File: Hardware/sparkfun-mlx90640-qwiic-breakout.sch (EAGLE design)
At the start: 23 parts, among them J2 SMD, J3 PTH, J4 SMD, U1 MLX90640

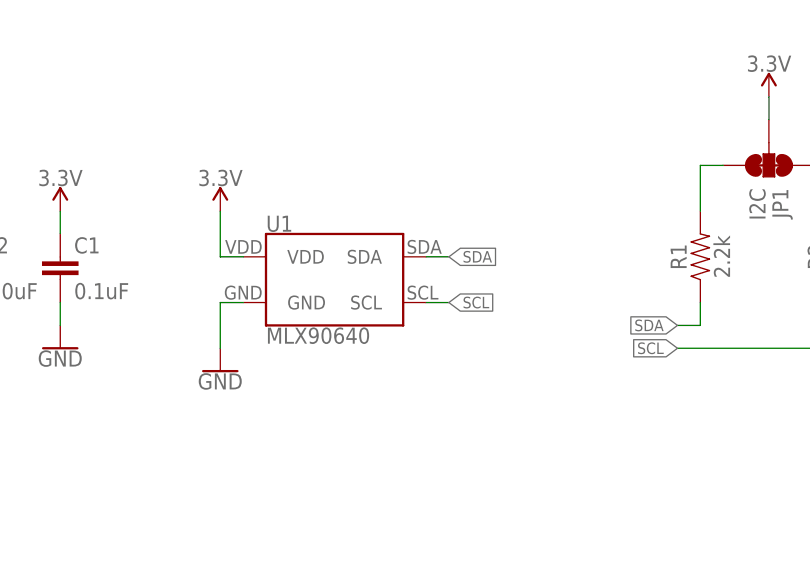
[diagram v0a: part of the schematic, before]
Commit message: Adding I2C address to schematic
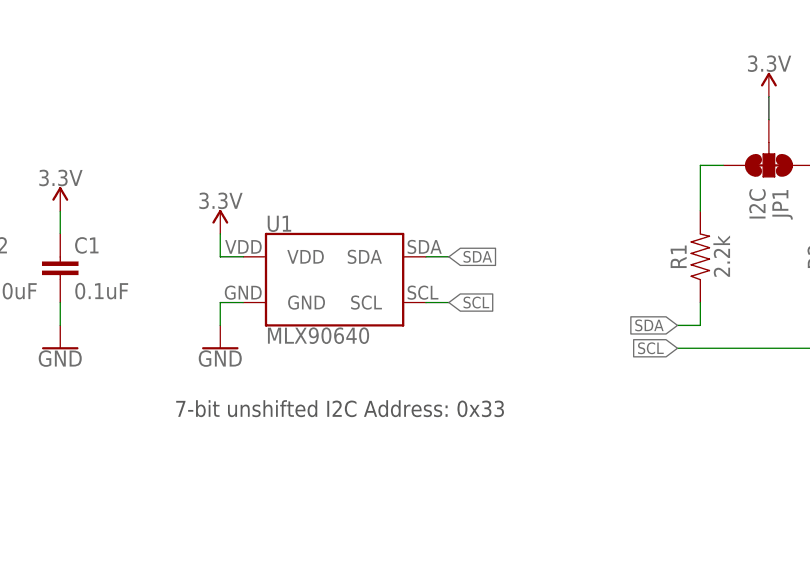
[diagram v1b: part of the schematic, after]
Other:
- note added: "7-bit unshifted I2C Address: 0x33"
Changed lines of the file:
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@@
 <grid distance="0.1" unitdist="inch" unit="inch" style="lines" multiple="1" display="no" altdistance="0.01" altunitdist="inch" altunit="inch"/>
 <layers>
-<layer number="1" name="Top" color="4" fill="1" visible="yes" active="no"/>
-<layer number="2" name="Route2" color="1" fill="3" visible="yes" active="no"/>
-<layer number="15" name="Route15" color="4" fill="6" visible="yes" active="no"/>
-<layer number="16" name="Bottom" color="1" fill="1" visible="yes" active="no"/>
-<layer number="17" name="Pads" color="2" fill="1" visible="yes" active="no"/>
-<layer number="18" name="Vias" color="2" fill="1" visible="yes" active="no"/>
-<layer number="19" name="Unrouted" color="6" fill="1" visible="yes" active="no"/>
-<layer number="20" name="Dimension" color="15" fill="1" visible="yes" active="no"/>
-<layer number="21" name="tPlace" color="16" fill="1" visible="yes" active="no"/>
-<layer number="22" name="bPlace" color="14" fill="1" visible="yes" active="no"/>
-<layer number="23" name="tOrigins" color="15" fill="1" visible="yes" active="no"/>
-<layer number="24" name="bOrigins" color="15" fill="1" visible="yes" active="no"/>
-<layer number="25" name="tNames" color="7" fill="1" visible="yes" active="no"/>
-<layer number="26" name="bNames" color="7" fill="1" visible="yes" active="no"/>
-<layer number="27" name="tValues" color="7" fill="1" visible="yes" active="no"/>
-<layer number="28" name="bValues" color="7" fill="1" visible="yes" active="no"/>
+<layer number="1" name="Top" color="4" fill="1" visible="no" active="no"/>
+<layer number="2" name="Route2" color="1" fill="3" visible="no" active="no"/>
+<layer number="15" name="Route15" color="4" fill="6" visible="no" active="no"/>
+<layer number="16" name="Bottom" color="1" fill="1" visible="no" active="no"/>
+<layer number="17" name="Pads" color="2" fill="1" visible="no" active="no"/>
+<layer number="18" name="Vias" color="2" fill="1" visible="no" active="no"/>
+<layer number="19" name="Unrouted" color="6" fill="1" visible="no" active="no"/>
+<layer number="20" name="Dimension" color="15" fill="1" visible="no" active="no"/>
+<layer number="21" name="tPlace" color="16" fill="1" visible="no" active="no"/>
+<layer number="22" name="bPlace" color="14" fill="1" visible="no" active="no"/>
+<layer number="23" name="tOrigins" color="15" fill="1" visible="no" active="no"/>
+<layer number="24" name="bOrigins" color="15" fill="1" visible="no" active="no"/>
+<layer number="25" name="tNames" color="7" fill="1" visible="no" active="no"/>
+<layer number="26" name="bNames" color="7" fill="1" visible="no" active="no"/>
+<layer number="27" name="tValues" color="7" fill="1" visible="no" active="no"/>
+<layer number="28" name="bValues" color="7" fill="1" visible="no" active="no"/>
 <layer number="29" name="tStop" color="7" fill="3" visible="no" active="no"/>
 <layer number="30" name="bStop" color="7" fill="6" visible="no" active="no"/>
@@
 <layer number="35" name="tGlue" color="7" fill="4" visible="no" active="no"/>
 <layer number="36" name="bGlue" color="7" fill="5" visible="no" active="no"/>
-<layer number="37" name="tTest" color="7" fill="1" visible="yes" active="no"/>
-<layer number="38" name="bTest" color="7" fill="1" visible="yes" active="no"/>
+<layer number="37" name="tTest" color="7" fill="1" visible="no" active="no"/>
+<layer number="38" name="bTest" color="7" fill="1" visible="no" active="no"/>
 <layer number="39" name="tKeepout" color="4" fill="11" visible="no" active="no"/>
 <layer number="40" name="bKeepout" color="1" fill="11" visible="no" active="no"/>
@@
 <layer number="44" name="Drills" color="7" fill="1" visible="no" active="no"/>
 <layer number="45" name="Holes" color="7" fill="1" visible="no" active="no"/>
-<layer number="46" name="Milling" color="3" fill="1" visible="yes" active="no"/>
-<layer number="47" name="Measures" color="7" fill="1" visible="yes" active="no"/>
-<layer number="48" name="Document" color="7" fill="1" visible="yes" active="no"/>
-<layer number="49" name="Reference" color="7" fill="1" visible="yes" active="no"/>
-<layer number="50" name="dxf" color="7" fill="1" visible="yes" active="no"/>
-<layer number="51" name="tDocu" color="6" fill="1" visible="yes" active="no"/>
-<layer number="52" name="bDocu" color="7" fill="1" visible="yes" active="no"/>
-<layer number="53" name="tGND_GNDA" color="7" fill="9" visible="yes" active="no"/>
-<layer number="54" name="bGND_GNDA" color="1" fill="9" visible="yes" active="no"/>
-<layer number="56" name="wert" color="7" fill="1" visible="yes" active="no"/>
-<layer number="57" name="tCAD" color="7" fill="1" visible="yes" active="no"/>
-<layer number="59" name="tCarbon" color="7" fill="1" visible="yes" active="no"/>
-<layer number="60" name="bCarbon" color="7" fill="1" visible="yes" active="no"/>
+<layer number="46" name="Milling" color="3" fill="1" visible="no" active="no"/>
+<layer number="47" name="Measures" color="7" fill="1" visible="no" active="no"/>
+<layer number="48" name="Document" color="7" fill="1" visible="no" active="no"/>
+<layer number="49" name="Reference" color="7" fill="1" visible="no" active="no"/>
+<layer number="50" name="dxf" color="7" fill="1" visible="no" active="no"/>
+<layer number="51" name="tDocu" color="6" fill="1" visible="no" active="no"/>
+<layer number="52" name="bDocu" color="7" fill="1" visible="no" active="no"/>
+<layer number="53" name="tGND_GNDA" color="7" fill="9" visible="no" active="no"/>
+<layer number="54" name="bGND_GNDA" color="1" fill="9" visible="no" active="no"/>
+<layer number="56" name="wert" color="7" fill="1" visible="no" active="no"/>
+<layer number="57" name="tCAD" color="7" fill="1" visible="no" active="no"/>
+<layer number="59" name="tCarbon" color="7" fill="1" visible="no" active="no"/>
+<layer number="60" name="bCarbon" color="7" fill="1" visible="no" active="no"/>
 <layer number="88" name="SimResults" color="9" fill="1" visible="yes" active="yes"/>
 <layer number="89" name="SimProbes" color="9" fill="1" visible="yes" active="yes"/>
@@
 <text x="206.248" y="129.286" size="1.778" layer="97">Power</text>
 <text x="165.354" y="11.43" size="2.54" layer="94">Jim Lindblom</text>
+<text x="48.26" y="76.2" size="1.778" layer="97">7-bit unshifted I2C Address: 0x33</text>
 </plain>
 <instances>
@@
 <instance part="C1" gate="G$1" x="35.56" y="91.44"/>
 <instance part="SUPPLY1" gate="G$1" x="35.56" y="99.06"/>
-<instance part="SUPPLY2" gate="G$1" x="53.34" y="99.06"/>
+<instance part="SUPPLY2" gate="G$1" x="53.34" y="96.52"/>
 <instance part="GND1" gate="1" x="35.56" y="83.82"/>
-<instance part="GND2" gate="1" x="53.34" y="81.28"/>
+<instance part="GND2" gate="1" x="53.34" y="83.82"/>
 <instance part="C2" gate="G$1" x="25.4" y="91.44"/>
 <instance part="SUPPLY3" gate="G$1" x="25.4" y="99.06"/>
@@
 <pinref part="SUPPLY2" gate="G$1" pin="3.3V"/>
 <wire x1="55.88" y1="93.98" x2="53.34" y2="93.98" width="0.1524" layer="91"/>
-<wire x1="53.34" y1="93.98" x2="53.34" y2="99.06" width="0.1524" layer="91"/>
+<wire x1="53.34" y1="93.98" x2="53.34" y2="96.52" width="0.1524" layer="91"/>
 </segment>
 <segment>
@@
 <pinref part="GND2" gate="1" pin="GND"/>
 <wire x1="55.88" y1="88.9" x2="53.34" y2="88.9" width="0.1524" layer="91"/>
-<wire x1="53.34" y1="88.9" x2="53.34" y2="83.82" width="0.1524" layer="91"/>
-</segment>
-<segment>
+<wire x1="53.34" y1="88.9" x2="53.34" y2="86.36" width="0.1524" layer="91"/>
+</segment>
+<segment>
